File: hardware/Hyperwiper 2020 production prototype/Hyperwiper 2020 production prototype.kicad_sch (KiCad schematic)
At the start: 20 parts, among them J1 Conn_01x05, Q2 2N3904, Q3 IRF4905, SW1 SW_DPDT_x2, SW2 SW_Reed, U1 Teensy4.0, U3 Voltage regulator

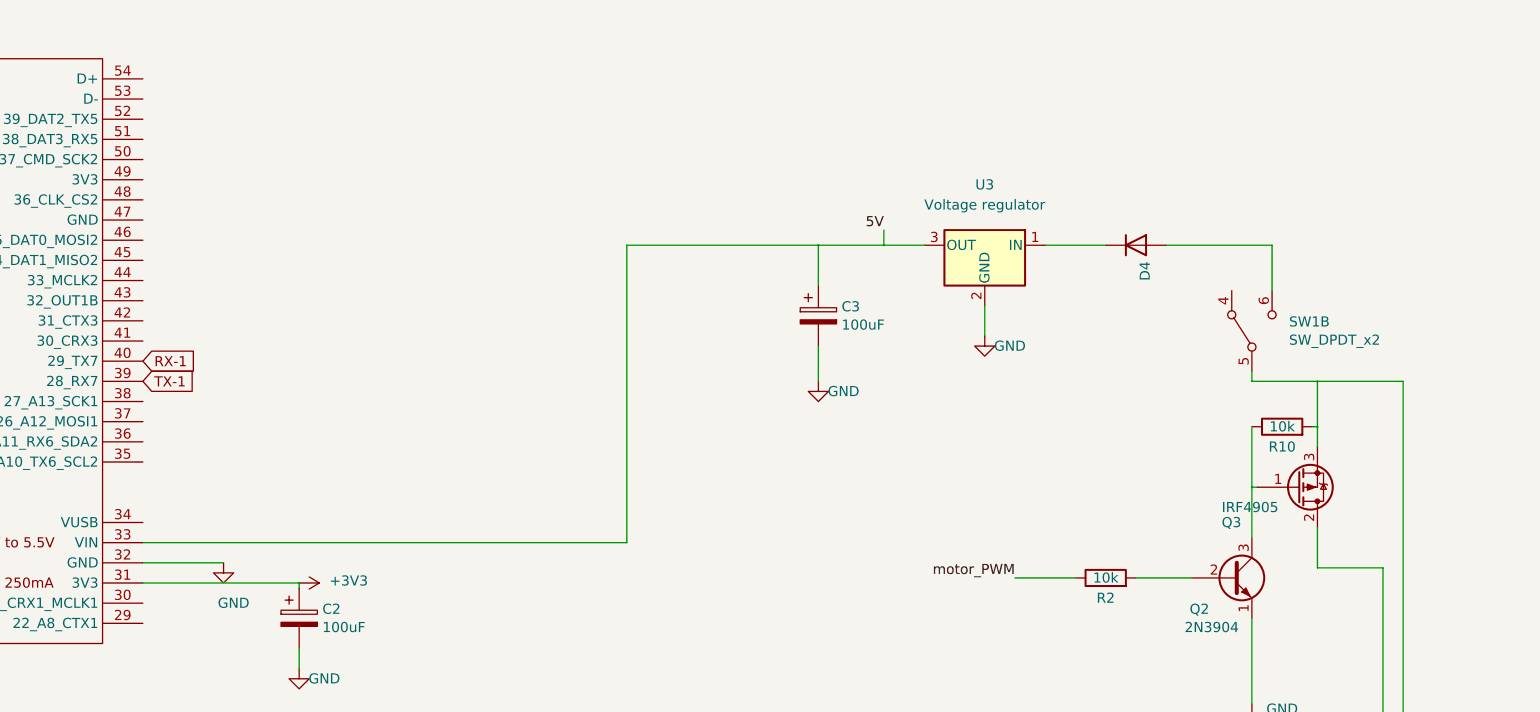
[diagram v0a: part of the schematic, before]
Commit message: Updated board to V2.4.0 with relay and usb out
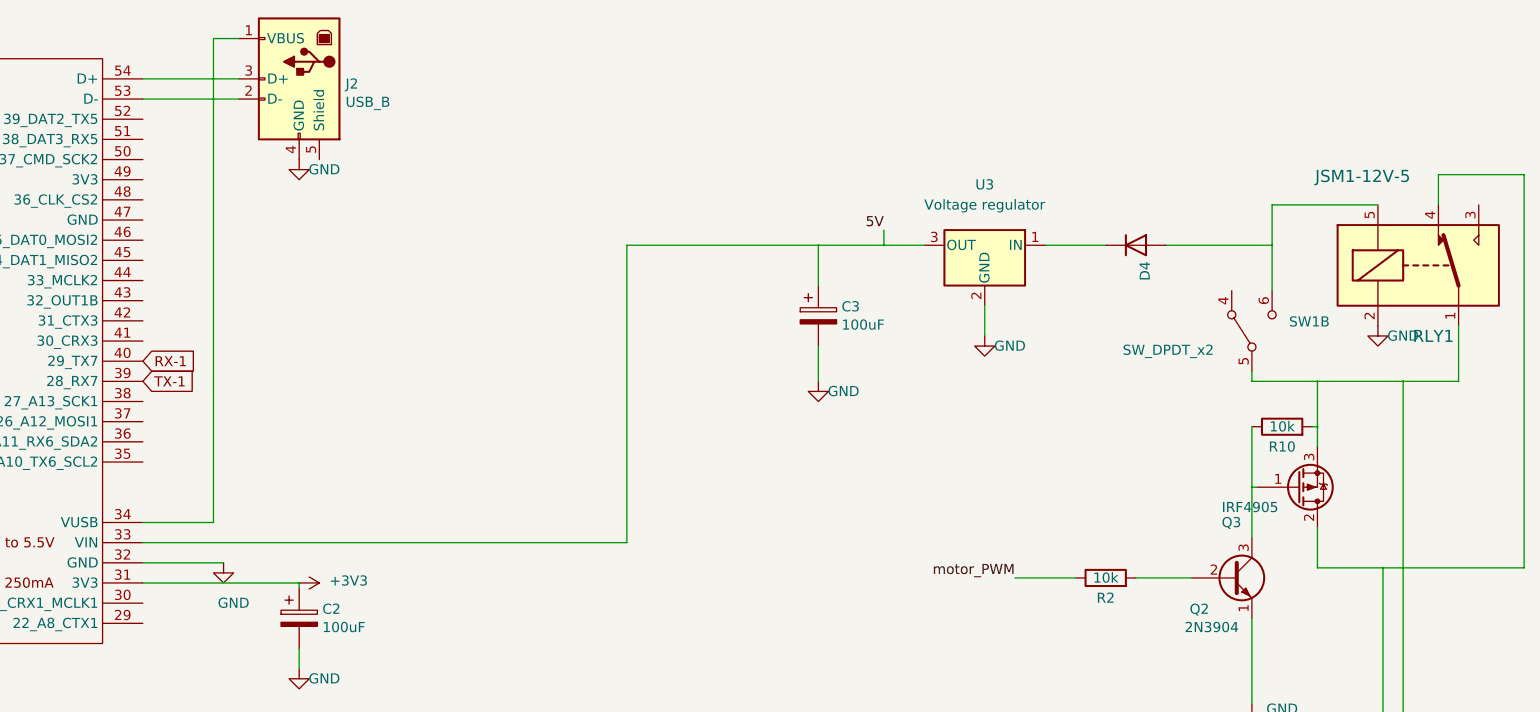
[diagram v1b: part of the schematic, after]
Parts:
- added J2: USB_B, Connector_USB:USB_Micro-B_Amphenol_10103594-0001LF_Horizontal, symbol Connector:USB_B
- added RLY1: JSM1-12V-5, Relay_THT:Relay_SPDT_SANYOU_SRD_Series_Form_C, symbol Relay:SANYOU_SRD_Form_C
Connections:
- net GND: now also J2.4 (GND), RLY1.2
- net at J1.1 (Pin_1), Q3.3 (S), R10.2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: now also RLY1.1
- net at D4.1 (A), SW1.6 (C): now also RLY1.5
- net at J1.2 (Pin_2), Q3.2 (D): now also RLY1.4
- net at U1.34 (VUSB): now also J2.1 (VBUS)
- net at U1.53 (D-): now also J2.2 (D-)
- net at U1.54 (D+): now also J2.3 (D+)
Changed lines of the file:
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@@
     (title "Prototype board")
     (date "2021-02-18")
-    (rev "V2.2.6")
+    (rev "V2.4.0")
   )
   (junction (at 127.635 88.9) (diameter 0.259) (color 0 0 0 0))
@@
   (junction (at 241.935 122.555) (diameter 0.259) (color 0 0 0 0))
   (junction (at 247.65 76.835) (diameter 0.259) (color 0 0 0 0))
+  (junction (at 250.19 46.355) (diameter 0.259) (color 0 0 0 0))
   (junction (at 255.905 63.5) (diameter 0.259) (color 0 0 0 0))
   (junction (at 255.905 69.215) (diameter 0.259) (color 0 0 0 0))
   (junction (at 261.62 113.03) (diameter 0.259) (color 0 0 0 0))
+  (junction (at 264.16 86.995) (diameter 0.259) (color 0 0 0 0))
+  (junction (at 266.7 63.5) (diameter 0.259) (color 0 0 0 0))
   (wire (pts (xy 43.815 116.84) (xy 46.355 116.84))
     (stroke (width 0) (type solid) (color 0 0 0 0))
@@
     (stroke (width 0) (type solid) (color 0 0 0 0))
   )
+  (wire (pts (xy 107.95 25.4) (xy 120.015 25.4))
+    (stroke (width 0) (type solid) (color 0 0 0 0))
+  )
+  (wire (pts (xy 107.95 27.94) (xy 120.015 27.94))
+    (stroke (width 0) (type solid) (color 0 0 0 0))
+  )
   (wire (pts (xy 107.95 83.82) (xy 168.91 83.82))
     (stroke (width 0) (type solid) (color 0 0 0 0))
@@
     (stroke (width 0) (type solid) (color 0 0 0 0))
   )
+  (wire (pts (xy 116.84 20.32) (xy 116.84 81.28))
+    (stroke (width 0) (type solid) (color 0 0 0 0))
+  )
+  (wire (pts (xy 116.84 81.28) (xy 107.95 81.28))
+    (stroke (width 0) (type solid) (color 0 0 0 0))
+  )
+  (wire (pts (xy 120.015 20.32) (xy 116.84 20.32))
+    (stroke (width 0) (type solid) (color 0 0 0 0))
+  )
   (wire (pts (xy 127.635 88.9) (xy 127.635 89.535))
     (stroke (width 0) (type solid) (color 0 0 0 0))
@@
     (stroke (width 0) (type solid) (color 0 0 0 0))
   )
+  (wire (pts (xy 250.19 41.275) (xy 250.19 46.355))
+    (stroke (width 0) (type solid) (color 0 0 0 0))
+  )
   (wire (pts (xy 250.19 46.355) (xy 250.19 52.07))
     (stroke (width 0) (type solid) (color 0 0 0 0))
@@
     (stroke (width 0) (type solid) (color 0 0 0 0))
   )
+  (wire (pts (xy 263.525 41.275) (xy 250.19 41.275))
+    (stroke (width 0) (type solid) (color 0 0 0 0))
+  )
   (wire (pts (xy 264.16 86.995) (xy 264.16 113.03))
     (stroke (width 0) (type solid) (color 0 0 0 0))
@@
   )
   (wire (pts (xy 266.7 120.65) (xy 266.7 128.27))
+    (stroke (width 0) (type solid) (color 0 0 0 0))
+  )
+  (wire (pts (xy 271.145 37.465) (xy 281.94 37.465))
+    (stroke (width 0) (type solid) (color 0 0 0 0))
+  )
+  (wire (pts (xy 271.145 41.275) (xy 271.145 37.465))
+    (stroke (width 0) (type solid) (color 0 0 0 0))
+  )
+  (wire (pts (xy 273.685 56.515) (xy 273.685 63.5))
+    (stroke (width 0) (type solid) (color 0 0 0 0))
+  )
+  (wire (pts (xy 273.685 63.5) (xy 266.7 63.5))
+    (stroke (width 0) (type solid) (color 0 0 0 0))
+  )
+  (wire (pts (xy 281.94 37.465) (xy 281.94 86.995))
+    (stroke (width 0) (type solid) (color 0 0 0 0))
+  )
+  (wire (pts (xy 281.94 86.995) (xy 264.16 86.995))
     (stroke (width 0) (type solid) (color 0 0 0 0))
   )
@@
     (pin "1")
   )
+  (symbol (lib_id "power:GND") (at 127.635 35.56 0) (unit 1)
+    (in_bom yes) (on_board yes)
+    (property "Reference" "#PWR0118" (id 0) (at 127.635 41.91 0)
+      (effects (font (size 1.27 1.27)) hide)
+    )
+    (property "Value" "GND" (id 1) (at 130.81 36.83 0))
+    (property "Footprint" "" (id 2) (at 127.635 35.56 0)
+      (effects (font (size 1.27 1.27)) hide)
+    )
+    (property "Datasheet" "" (id 3) (at 127.635 35.56 0)
+      (effects (font (size 1.27 1.27)) hide)
+    )
+    (pin "1")
+  )
   (symbol (lib_id "power:GND") (at 127.635 99.695 0) (unit 1)
     (in_bom yes) (on_board yes)
@@
     )
     (property "Datasheet" "" (id 3) (at 261.62 143.51 0)
+      (effects (font (size 1.27 1.27)) hide)
+    )
+    (pin "1")
+  )
+  (symbol (lib_id "power:GND") (at 263.525 56.515 0) (unit 1)
+    (in_bom yes) (on_board yes)
+    (property "Reference" "#PWR01" (id 0) (at 263.525 62.865 0)
+      (effects (font (size 1.27 1.27)) hide)
+    )
+    (property "Value" "GND" (id 1) (at 266.7 57.785 0))
+    (property "Footprint" "" (id 2) (at 263.525 56.515 0)
+      (effects (font (size 1.27 1.27)) hide)
+    )
+    (property "Datasheet" "" (id 3) (at 263.525 56.515 0)
       (effects (font (size 1.27 1.27)) hide)
     )
@@
       (effects (font (size 1.27 1.27)) (justify right))
     )
-    (property "Value" "SW_DPDT_x2" (id 1) (at 252.3237 58.2993 90)
+    (property "Value" "SW_DPDT_x2" (id 1) (at 231.3687 59.5693 90)
       (effects (font (size 1.27 1.27)) (justify right))
     )
@@
     (pin "8")
     (pin "9")
+  )
+  (symbol (lib_id "Connector:USB_B") (at 127.635 25.4 0) (mirror y) (unit 1)
+    (in_bom yes) (on_board yes) (fields_autoplaced)
+    (property "Reference" "J2" (id 0) (at 133.4771 26.0361 0)
+      (effects (font (size 1.27 1.27)) (justify right))
+    )
+    (property "Value" "USB_B" (id 1) (at 133.4771 28.3348 0)
+      (effects (font (size 1.27 1.27)) (justify right))
+    )
+    (property "Footprint" "Connector_USB:USB_Micro-B_Amphenol_10103594-0001LF_Horizontal" (id 2) (at 123.825 26.67 0)
+      (effects (font (size 1.27 1.27)) hide)
+    )
+    (property "Datasheet" "https://www.digikey.com/en/products/detail/amphenol-icc-fci/10118194-0001LF/2785389" (id 3) (at 123.825 26.67 0)
+      (effects (font (size 1.27 1.27)) hide)
+    )
+    (pin "1")
+    (pin "2")
+    (pin "3")
+    (pin "4")
+    (pin "5")
+  )
+  (symbol (lib_id "Relay:SANYOU_SRD_Form_C") (at 268.605 48.895 0) (unit 1)
+    (in_bom yes) (on_board yes)
+    (property "Reference" "RLY1" (id 0) (at 270.51 57.8309 0)
+      (effects (font (size 1.524 1.524)))
+    )
+    (property "Value" "JSM1-12V-5" (id 1) (at 261.62 37.6785 0)
+      (effects (font (size 1.524 1.524)))
+    )
+    (property "Footprint" "Relay_THT:Relay_SPDT_SANYOU_SRD_Series_Form_C" (id 2) (at 280.035 50.165 0)
+      (effects (font (size 1.27 1.27)) (justify left) hide)
+    )
+    (property "Datasheet" "http://www.sanyourelay.ca/public/products/pdf/SRD.pdf" (id 3) (at 268.605 48.895 0)
+      (effects (font (size 1.27 1.27)) hide)
+    )
+    (property "Digi-Key_PN" "255-1240-ND" (id 4) (at 273.685 38.735 0)
+      (effects (font (size 1.524 1.524)) (justify left) hide)
+    )
+    (property "MPN" "JSM1-12V-5" (id 5) (at 273.685 36.195 0)
+      (effects (font (size 1.524 1.524)) (justify left) hide)
+    )
+    (property "Category" "Relays" (id 6) (at 273.685 33.655 0)
+      (effects (font (size 1.524 1.524)) (justify left) hide)
+    )
+    (property "Family" "Automotive Relays" (id 7) (at 273.685 31.115 0)
+      (effects (font (size 1.524 1.524)) (justify left) hide)
+    )
+    (property "DK_Datasheet_Link" "https://media.digikey.com/pdf/Data%20Sheets/Panasonic%20Electric%20Works%20PDFs/JS-M_Series_Rev_Dec_2011.pdf" (id 8) (at 273.685 28.575 0)
+      (effects (font (size 1.524 1.524)) (justify left) hide)
+    )
+    (property "DK_Detail_Page" "/product-detail/en/panasonic-electric-works/JSM1-12V-5/255-1240-ND/274764" (id 9) (at 273.685 26.035 0)
+      (effects (font (size 1.524 1.524)) (justify left) hide)
+    )
+    (property "Description" "RELAY AUTOMOTIVE SPDT 15A 12V" (id 10) (at 273.685 23.495 0)
+      (effects (font (size 1.524 1.524)) (justify left) hide)
+    )
+    (property "Manufacturer" "Panasonic Electric Works" (id 11) (at 273.685 20.955 0)
+      (effects (font (size 1.524 1.524)) (justify left) hide)
+    )
+    (property "Status" "Active" (id 12) (at 273.685 18.415 0)
+      (effects (font (size 1.524 1.524)) (justify left) hide)
+    )
+    (pin "1")
+    (pin "2")
+    (pin "3")
+    (pin "4")
+    (pin "5")
   )
   (symbol (lib_id "SparkFun-RF:XBEE") (at 64.135 124.46 0) (unit 1)
@@
   )
   (symbol_instances
+    (path "/43d20774-dcf0-40f3-86c3-b53fd5e41616"
+      (reference "#PWR01") (unit 1) (value "GND") (footprint "")
+    )
     (path "/1523e18f-a60a-446e-95ea-88795e5fc309"
       (reference "#PWR02") (unit 1) (value "GND") (footprint "")
@@
       (reference "#PWR0117") (unit 1) (value "GND") (footprint "")
     )
+    (path "/11df51f8-67e8-4efd-bac0-3078efeac09f"
+      (reference "#PWR0118") (unit 1) (value "GND") (footprint "")
+    )
     (path "/bc80e3ce-b48d-40fd-b22c-6384e7899540"
       (reference "C1") (unit 1) (value "0.1uF") (footprint "Capacitor_THT:C_Rect_L7.0mm_W2.5mm_P5.00mm")
@@
       (reference "J1") (unit 1) (value "Conn_01x05") (footprint "TerminalBlock_MetzConnect:TerminalBlock_MetzConnect_Type011_RT05505HBWC_1x05_P5.00mm_Horizontal")
     )
+    (path "/b2ed6726-d6be-49ad-bfde-2fa1b7fc0736"
+      (reference "J2") (unit 1) (value "USB_B") (footprint "Connector_USB:USB_Micro-B_Amphenol_10103594-0001LF_Horizontal")
+    )
     (path "/e866b7a7-861f-4eaf-84b8-bf844f4ad0ac"
       (reference "JP1") (unit 1) (value "XBEE 1") (footprint "RF_Module:Xbee")
@@
       (reference "R10") (unit 1) (value "10k") (footprint "Resistor_THT:R_Axial_DIN0207_L6.3mm_D2.5mm_P10.16mm_Horizontal")
     )
+    (path "/9655f52e-d83d-4b34-981f-5781f9027fde"
+      (reference "RLY1") (unit 1) (value "JSM1-12V-5") (footprint "Relay_THT:Relay_SPDT_SANYOU_SRD_Series_Form_C")
+    )
     (path "/d1f2e322-a42b-493d-8e40-7f912a67ae28"
